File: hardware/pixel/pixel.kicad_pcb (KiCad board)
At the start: 2 copper layers, 20 x 20 mm, 13 parts, among them J1 IN (male), J2 OUT (female), U1 WS2814F

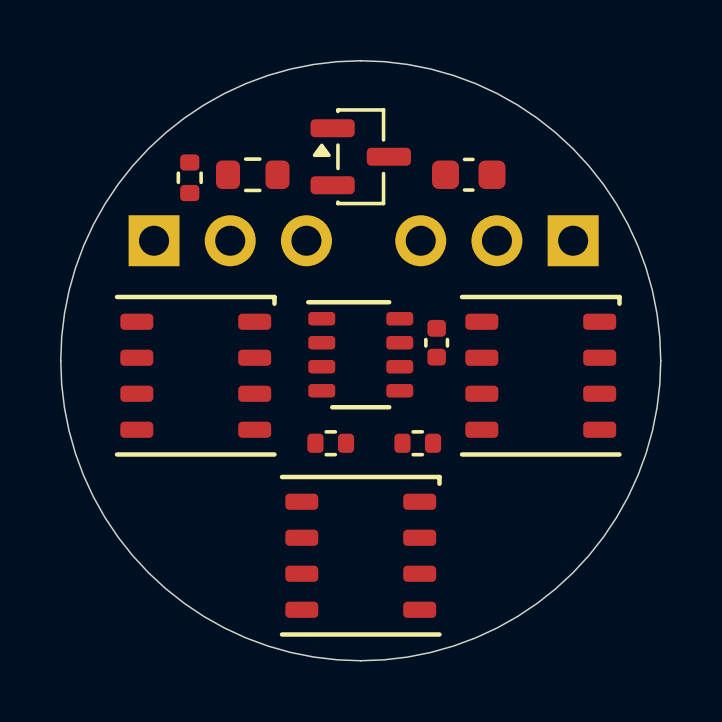
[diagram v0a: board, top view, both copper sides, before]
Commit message: Pixel PCB: rotate LEDs so each group of LED nets fans without crossing
The LED chain +12V -> D2 -> D3 -> D4 -> U1 now runs east -> south -> west.
D2 (rot 90) sends its cathodes south to D3's anode column, and D3
(rot 0) sends its cathodes west to D4's anode row. D4 (rot 270) puts
its R/G/B cathodes directly below U1's matching output pins. U1 moves
up, and R4, C1 and R3 are re-fitted. Placement score 100.

Co-Authored-By: Claude Opus 5.5 <noreply@anthropic.com>
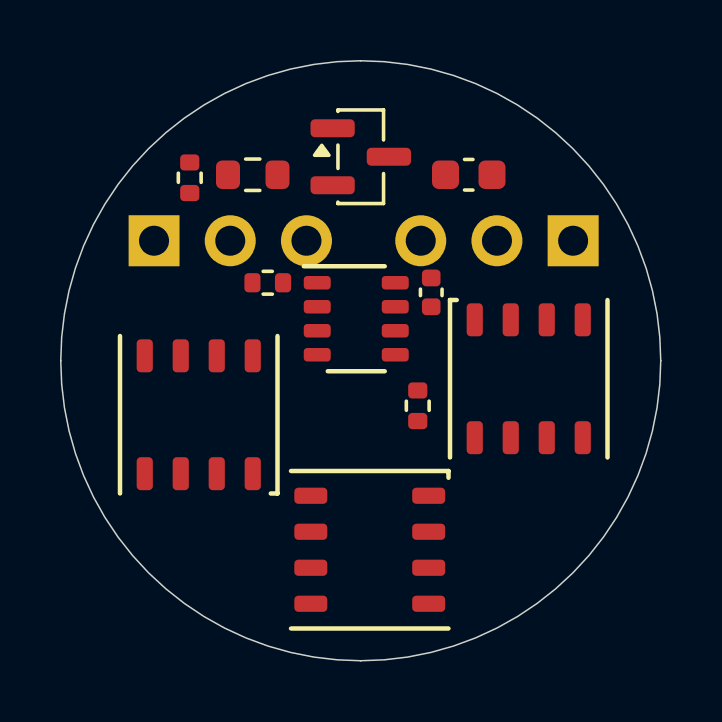
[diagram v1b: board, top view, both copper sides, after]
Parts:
- moved D2 8.13 mm to (105.6, 100.6), turned to 90 degrees
- moved D3 8.13 mm to (100.3, 106.3)
- moved R4 5.75 mm to (96.9, 97.4)
- moved C1 1.69 mm to (102.3, 97.7)
- moved D4 1.30 mm to (94.6, 101.8), turned to -90 degrees
- moved R3 1.25 mm to (101.9, 101.5), turned to 90 degrees
- moved U1 1.21 mm to (99.8, 98.6)
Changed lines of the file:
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@@
 	(footprint "village:FSOP-8_1.65x3.25mm_P0.8mm"
 		(layer "F.Cu")
-		(at 100 99.8)
+		(at 99.85 98.6)
 		(descr "FSOP-8, 1.65x3.25mm body, 0.8mm pitch, 2.85mm lead span (Worldsemi WS2814F, datasheet V1.1 p.6). Land: 0.9x0.45mm pads, 0.3mm toe / 0.2mm heel. Not yet verified on a fabricated board.")
 		(property "Reference" "U1"
@@
 			(stroke
 				(width 0.15)
-				(type default)
+				(type solid)
 			)
 			(layer "F.SilkS")
@@
 			(stroke
 				(width 0.15)
-				(type default)
+				(type solid)
 			)
 			(layer "F.SilkS")
@@
 			(stroke
 				(width 0.05)
-				(type default)
+				(type solid)
 			)
 			(fill no)
@@
 			(stroke
 				(width 0.1)
-				(type default)
+				(type solid)
 			)
 			(fill no)
@@
 	(footprint "village:LED_Honglitronic_HL-5050RGBW_5.0x5.0mm_P1.2mm"
 		(layer "F.Cu")
-		(at 106 100.5)
+		(at 100.3 106.3)
 		(descr "RGBW 5050 LED, 8 pads, Honglitronic HL-5050RGBW-S1 (spec B-18-A-1651 rev A/2 p.3), recommended land pattern: 1.1x0.54mm pads, 2.83mm inner gap, 1.2mm pitch. Top view: anodes 1/3/5/7 (W/B/G/R) on the right, cathodes 2/4/6/8 on the left; the part's corner mark is at pin 2. Datasheet top and bottom views disagree on mirroring: verify on a sample before fab.")
 		(property "Reference" "D3"
@@
 			(stroke
 				(width 0.15)
-				(type default)
+				(type solid)
 			)
 			(layer "F.SilkS")
@@
 			(stroke
 				(width 0.15)
-				(type default)
+				(type solid)
 			)
 			(layer "F.SilkS")
@@
 			(stroke
 				(width 0.15)
-				(type default)
+				(type solid)
 			)
 			(layer "F.SilkS")
@@
 			(stroke
 				(width 0.05)
-				(type default)
+				(type solid)
 			)
 			(fill no)
@@
 			(stroke
 				(width 0.1)
-				(type default)
+				(type solid)
 			)
 			(fill no)
@@
 	(footprint "Capacitor_SMD:C_0402_1005Metric"
 		(layer "F.Cu")
-		(at 102.53 99.4 90)
+		(at 102.35 97.72 90)
 		(descr "Capacitor SMD 0402 (1005 Metric), square (rectangular) end terminal, IPC-7351 nominal, (Body size source: IPC-SM-782 page 76, https://www.pcb-3d.com/wordpress/wp-content/uploads/ipc-sm-782a_amendment_1_and_2.pdf)")
 		(tags "capacitor")
@@
 	(footprint "village:LED_Honglitronic_HL-5050RGBW_5.0x5.0mm_P1.2mm"
 		(layer "F.Cu")
-		(at 94.5 100.5)
+		(at 94.6 101.8 -90)
 		(descr "RGBW 5050 LED, 8 pads, Honglitronic HL-5050RGBW-S1 (spec B-18-A-1651 rev A/2 p.3), recommended land pattern: 1.1x0.54mm pads, 2.83mm inner gap, 1.2mm pitch. Top view: anodes 1/3/5/7 (W/B/G/R) on the right, cathodes 2/4/6/8 on the left; the part's corner mark is at pin 2. Datasheet top and bottom views disagree on mirroring: verify on a sample before fab.")
 		(property "Reference" "D4"
-			(at 0 -1 0)
+			(at 0 -1 -90)
 			(unlocked yes)
 			(layer "F.SilkS")
@@
 		)
 		(property "Value" "HL-5050RGBW-S1-A27"
-			(at 0 1 0)
+			(at 0 1 -90)
 			(unlocked yes)
 			(layer "F.SilkS")
@@
 		)
 		(property "Datasheet" ""
-			(at 0 0 0)
+			(at 0 0 -90)
 			(layer "F.Fab")
 			(hide yes)
@@
 		)
 		(property "Description" ""
-			(at 0 0 0)
+			(at 0 0 -90)
 			(layer "F.Fab")
 			(hide yes)
@@
 		(duplicate_pad_numbers_are_jumpers no)
 		(fp_line
+			(start -2.625 2.625)
+			(end 2.625 2.625)
+			(stroke
+				(width 0.15)
+				(type solid)
+			)
+			(layer "F.SilkS")
+		)
+		(fp_line
 			(start -2.625 -2.625)
 			(end 2.625 -2.625)
 			(stroke
 				(width 0.15)
-				(type default)
-			)
-			(layer "F.SilkS")
-		)
-		(fp_line
-			(start -2.625 2.625)
-			(end 2.625 2.625)
-			(stroke
-				(width 0.15)
-				(type default)
+				(type solid)
 			)
 			(layer "F.SilkS")
@@
 			(stroke
 				(width 0.15)
-				(type default)
+				(type solid)
 			)
 			(layer "F.SilkS")
@@
 			(stroke
 				(width 0.05)
-				(type default)
+				(type solid)
 			)
 			(fill no)
@@
 			(stroke
 				(width 0.1)
-				(type default)
+				(type solid)
 			)
 			(fill no)
@@
 		)
 		(pad "1" smd roundrect
-			(at 1.965 -1.8)
+			(at 1.965 -1.8 270)
 			(size 1.1 0.54)
 			(layers "F.Cu" "F.Mask" "F.Paste")
@@
 		)
 		(pad "2" smd roundrect
-			(at -1.965 -1.8)
+			(at -1.965 -1.8 270)
 			(size 1.1 0.54)
 			(layers "F.Cu" "F.Mask" "F.Paste")
@@
 		)
 		(pad "3" smd roundrect
-			(at 1.965 -0.6)
+			(at 1.965 -0.6 270)
 			(size 1.1 0.54)
 			(layers "F.Cu" "F.Mask" "F.Paste")
@@
 		)
 		(pad "4" smd roundrect
-			(at -1.965 -0.6)
+			(at -1.965 -0.6 270)
 			(size 1.1 0.54)
 			(layers "F.Cu" "F.Mask" "F.Paste")
@@
 		)
 		(pad "5" smd roundrect
-			(at 1.965 0.6)
+			(at 1.965 0.6 270)
 			(size 1.1 0.54)
 			(layers "F.Cu" "F.Mask" "F.Paste")
@@
 		)
 		(pad "6" smd roundrect
-			(at -1.965 0.6)
+			(at -1.965 0.6 270)
 			(size 1.1 0.54)
 			(layers "F.Cu" "F.Mask" "F.Paste")
@@
 		)
 		(pad "7" smd roundrect
-			(at 1.965 1.8)
+			(at 1.965 1.8 270)
 			(size 1.1 0.54)
 			(layers "F.Cu" "F.Mask" "F.Paste")
@@
 		)
 		(pad "8" smd roundrect
-			(at -1.965 1.8)
+			(at -1.965 1.8 270)
 			(size 1.1 0.54)
 			(layers "F.Cu" "F.Mask" "F.Paste")
@@
 	(footprint "village:LED_Honglitronic_HL-5050RGBW_5.0x5.0mm_P1.2mm"
 		(layer "F.Cu")
-		(at 100 106.5)
+		(at 105.6 100.6 90)
 		(descr "RGBW 5050 LED, 8 pads, Honglitronic HL-5050RGBW-S1 (spec B-18-A-1651 rev A/2 p.3), recommended land pattern: 1.1x0.54mm pads, 2.83mm inner gap, 1.2mm pitch. Top view: anodes 1/3/5/7 (W/B/G/R) on the right, cathodes 2/4/6/8 on the left; the part's corner mark is at pin 2. Datasheet top and bottom views disagree on mirroring: verify on a sample before fab.")
 		(property "Reference" "D2"
-			(at 0 -1 0)
+			(at 0 -1 90)
 			(unlocked yes)
 			(layer "F.SilkS")
@@
 		)
 		(property "Value" "HL-5050RGBW-S1-A27"
-			(at 0 1 0)
+			(at 0 1 90)
 			(unlocked yes)
 			(layer "F.SilkS")
@@
 		)
 		(property "Datasheet" ""
-			(at 0 0 0)
+			(at 0 0 90)
 			(layer "F.Fab")
 			(hide yes)
@@
 		)
 		(property "Description" ""
-			(at 0 0 0)
+			(at 0 0 90)
 			(layer "F.Fab")
 			(hide yes)
@@
 		(duplicate_pad_numbers_are_jumpers no)
 		(fp_line
+			(start 2.625 -2.625)
+			(end 2.625 -2.4)
+			(stroke
+				(width 0.15)
+				(type solid)
+			)
+			(layer "F.SilkS")
+		)
+		(fp_line
 			(start -2.625 -2.625)
 			(end 2.625 -2.625)
 			(stroke
 				(width 0.15)
-				(type default)
+				(type solid)
 			)
 			(layer "F.SilkS")
@@
 			(stroke
 				(width 0.15)
-				(type default)
-			)
-			(layer "F.SilkS")
-		)
-		(fp_line
-			(start 2.625 -2.625)
-			(end 2.625 -2.4)
-			(stroke
-				(width 0.15)
-				(type default)
+				(type solid)
 			)
 			(layer "F.SilkS")
@@
 			(stroke
 				(width 0.05)
-				(type default)
+				(type solid)
 			)
 			(fill no)
@@
 			(stroke
 				(width 0.1)
-				(type default)
+				(type solid)
 			)
 			(fill no)
@@
 		)
 		(pad "1" smd roundrect
-			(at 1.965 -1.8)
+			(at 1.965 -1.8 90)
 			(size 1.1 0.54)
 			(layers "F.Cu" "F.Mask" "F.Paste")
@@
 		)
 		(pad "2" smd roundrect
-			(at -1.965 -1.8)
+			(at -1.965 -1.8 90)
 			(size 1.1 0.54)
 			(layers "F.Cu" "F.Mask" "F.Paste")
@@
 		)
 		(pad "3" smd roundrect
-			(at 1.965 -0.6)
+			(at 1.965 -0.6 90)
 			(size 1.1 0.54)
 			(layers "F.Cu" "F.Mask" "F.Paste")
@@
 		)
 		(pad "4" smd roundrect
-			(at -1.965 -0.6)
+			(at -1.965 -0.6 90)
 			(size 1.1 0.54)
 			(layers "F.Cu" "F.Mask" "F.Paste")
@@
 		)
 		(pad "5" smd roundrect
-			(at 1.965 0.6)
+			(at 1.965 0.6 90)
 			(size 1.1 0.54)
 			(layers "F.Cu" "F.Mask" "F.Paste")
@@
 		)
 		(pad "6" smd roundrect
-			(at -1.965 0.6)
+			(at -1.965 0.6 90)
 			(size 1.1 0.54)
 			(layers "F.Cu" "F.Mask" "F.Paste")
@@
 		)
 		(pad "7" smd roundrect
-			(at 1.965 1.8)
+			(at 1.965 1.8 90)
 			(size 1.1 0.54)
 			(layers "F.Cu" "F.Mask" "F.Paste")
@@
 		)
 		(pad "8" smd roundrect
-			(at -1.965 1.8)
+			(at -1.965 1.8 90)
 			(size 1.1 0.54)
 			(layers "F.Cu" "F.Mask" "F.Paste")
@@
 	(footprint "Resistor_SMD:R_0402_1005Metric"
 		(layer "F.Cu")
-		(at 101.9 102.75)
+		(at 101.9 101.5 90)
 		(descr "Resistor SMD 0402 (1005 Metric), square (rectangular) end terminal, IPC-7351 nominal, (Body size source: IPC-SM-782 page 72, https://www.pcb-3d.com/wordpress/wp-content/uploads/ipc-sm-782a_amendment_1_and_2.pdf)")
 		(tags "resistor")
 		(property "Reference" "R3"
-			(at 0 -1.17 0)
+			(at 0 -1.17 90)
 			(unlocked yes)
 			(layer "F.SilkS")
@@
 		)
 		(property "Value" "100"
-			(at 0 1.170001 0)
+			(at 0 1.170001 90)
 			(unlocked yes)
 			(layer "F.SilkS")
@@
 		)
 		(property "Datasheet" ""
-			(at 0 0 0)
+			(at 0 0 90)
 			(layer "F.Fab")
 			(hide yes)
@@
 		)
 		(property "Description" ""
-			(at 0 0 0)
+			(at 0 0 90)
 			(layer "F.Fab")
 			(hide yes)
@@
 		)
 		(property "KiLib_Generator" "SMD_2terminal_chip_molded"
-			(at 0 0 0)
+			(at 0 0 90)
 			(unlocked yes)
 			(layer "F.SilkS")
@@
 		)
 		(fp_text user "${REFERENCE}"
-			(at 0 0 0)
+			(at 0 0 90)
 			(unlocked yes)
 			(layer "F.Fab")
@@
 		)
 		(pad "1" smd roundrect
-			(at -0.51 0)
+			(at -0.51 0 90)
 			(size 0.54 0.64)
 			(layers "F.Cu" "F.Mask" "F.Paste")
@@
 		)
 		(pad "2" smd roundrect
-			(at 0.51 0)
+			(at 0.51 0 90)
 			(size 0.54 0.64)
 			(layers "F.Cu" "F.Mask" "F.Paste")
@@
 	(footprint "Resistor_SMD:R_0402_1005Metric"
 		(layer "F.Cu")
-		(at 99 102.75)
+		(at 96.9 97.4)
 		(descr "Resistor SMD 0402 (1005 Metric), square (rectangular) end terminal, IPC-7351 nominal, (Body size source: IPC-SM-782 page 72, https://www.pcb-3d.com/wordpress/wp-content/uploads/ipc-sm-782a_amendment_1_and_2.pdf)")
 		(tags "resistor")

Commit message: Pixel PCB: route with Freerouting
Autorouted with Freerouting 2.4.1: 88 segments, 4 vias, 0.4 mm on
+12V/GND. The LED groups fan diagonally between the rotated
LEDs. VDD narrows to 0.15 mm around U1, so the board minimum track
width is now 0.15 mm (JLCPCB's typical signal width; their limit is
0.10 mm). DRC: 0 errors, 0 unconnected.

Co-Authored-By: Claude Opus 5.5 <noreply@anthropic.com>
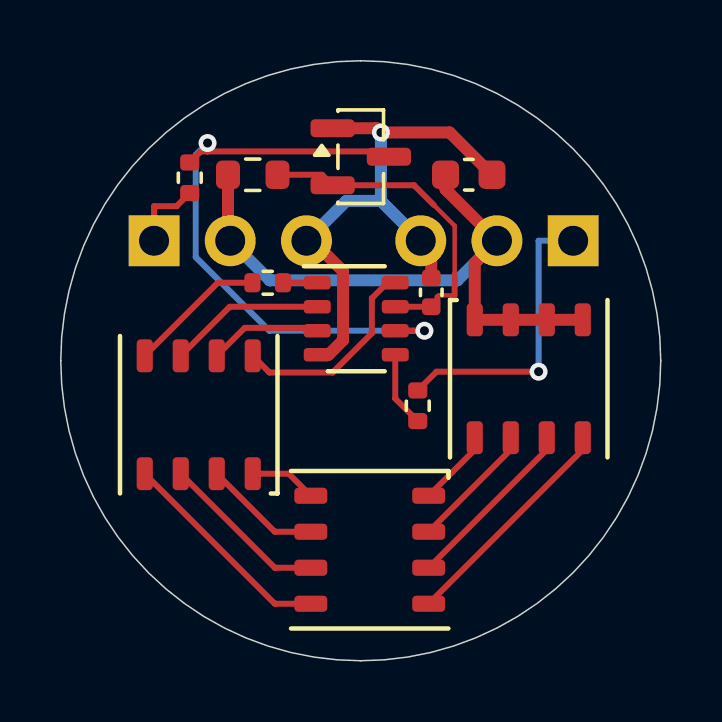
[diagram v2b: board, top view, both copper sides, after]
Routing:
- net +12V: track 0.00 -> 21.7 mm
- net /DIN: track 0.00 -> 20.7 mm, vias 0 -> 2
- net GND: track 0.00 -> 19.5 mm, vias 0 -> 1
- net /VDD: track 0.00 -> 11.1 mm
- net /DATA_OUT: track 0.00 -> 9.80 mm, vias 0 -> 1
- net /RED1_K: track 0.00 -> 7.66 mm
- net /RED2_K: track 0.00 -> 7.33 mm
- net /OUTW: track 0.00 -> 6.90 mm
- net /GRN1_K: track 0.00 -> 5.96 mm
- net /GRN2_K: track 0.00 -> 5.63 mm
- net /OUTG: track 0.00 -> 5.23 mm
- net /RED3_K: track 0.00 -> 4.60 mm
- net /BLU1_K: track 0.00 -> 4.27 mm
- net /BLU2_K: track 0.00 -> 3.94 mm
- net /OUTB: track 0.00 -> 3.78 mm
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
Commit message: Pixel PCB: silkscreen markings for plugging in and JLCPCB assembly review
Bottom: pin-1 (data) triangles and +/- marks at each header (shapes, so
they read correctly on the back), and a JLCJLCJLCJLC order-number
placeholder. Top: revision v0.1, and a pin-1 dot inside U1 because J1's
pad clips the footprint's own pin-1 line. The schematic note no
longer lists the footprints as TBD. DRC: 0 errors; ERC clean.

Co-Authored-By: Claude Opus 5.5 <noreply@anthropic.com>
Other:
- board text added: "JLCJLCJLCJLC"
- board text added: "v0.1"
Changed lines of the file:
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@@
 		)
+	)
+	(gr_poly
+		(pts
+			(xy 99.267624 97.27) (xy 99.301227 97.284022) (xy 99.315249 97.317624) (xy 99.301227 97.351227) (xy 99.267624 97.365249)
+			(xy 99.234022 97.351227) (xy 99.22 97.317624) (xy 99.234022 97.284022)
+		)
+		(stroke
+			(width 0)
+			(type default)
+		)
+		(fill yes)
+		(layer "F.SilkS")
+	)
+	(gr_poly
+		(pts
+			(xy 92.71 94.3) (xy 92.921666 94.3) (xy 92.815833 94.471979)
+		)
+		(stroke
+			(width 0)
+			(type default)
+		)
+		(fill yes)
+		(layer "B.SilkS")
+	)
+	(gr_poly
+		(pts
+			(xy 106.68 94.3) (xy 106.891666 94.3) (xy 106.785833 94.471979)
+		)
+		(stroke
+			(width 0)
+			(type default)
+		)
+		(fill yes)
+		(layer "B.SilkS")
+	)
+	(gr_poly
+		(pts
+			(xy 97.79 94.26) (xy 98.001666 94.26) (xy 98.001666 94.307624) (xy 97.79 94.307624)
+		)
+		(stroke
+			(width 0)
+			(type default)
+		)
+		(fill yes)
+		(layer "B.SilkS")
+	)
+	(gr_poly
+		(pts
+			(xy 101.6 94.26) (xy 101.811666 94.26) (xy 101.811666 94.307624) (xy 101.6 94.307624)
+		)
+		(stroke
+			(width 0)
+			(type default)
+		)
+		(fill yes)
+		(layer "B.SilkS")
+	)
+	(gr_poly
+		(pts
+			(xy 95.33202 93.95) (xy 95.379645 93.95) (xy 95.379645 94.03202) (xy 95.461666 94.03202) (xy 95.461666 94.079645)
+			(xy 95.379645 94.079645) (xy 95.379645 94.161666) (xy 95.33202 94.161666) (xy 95.33202 94.079645)
+			(xy 95.25 94.079645) (xy 95.25 94.03202) (xy 95.33202 94.03202)
+		)
+		(stroke
+			(width 0)
+			(type default)
+		)
+		(fill yes)
+		(layer "B.SilkS")
+	)
+	(gr_poly
+		(pts
+			(xy 104.22202 93.95) (xy 104.269645 93.95) (xy 104.269645 94.03202) (xy 104.351666 94.03202) (xy 104.351666 94.079645)
+			(xy 104.269645 94.079645) (xy 104.269645 94.161666) (xy 104.22202 94.161666) (xy 104.22202 94.079645)
+			(xy 104.14 94.079645) (xy 104.14 94.03202) (xy 104.22202 94.03202)
+		)
+		(stroke
+			(width 0)
+			(type default)
+		)
+		(fill yes)
+		(layer "B.SilkS")
 	)
 	(gr_arc
@@
 		(layer "Edge.Cuts")
 	)
+	(gr_text "v0.1"
+		(at 105.4 105.9 0)
+		(layer "F.SilkS")
+		(effects
+			(font
+				(size 1 1)
+				(thickness 0.15)
+			)
+		)
+	)
+	(gr_text "JLCJLCJLCJLC"
+		(at 100 107.4 0)
+		(layer "B.SilkS")
+		(effects
+			(font
+				(size 1 1)
+				(thickness 0.15)
+			)
+		)
+	)
 	(segment
